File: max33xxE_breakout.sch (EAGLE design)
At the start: 12 parts

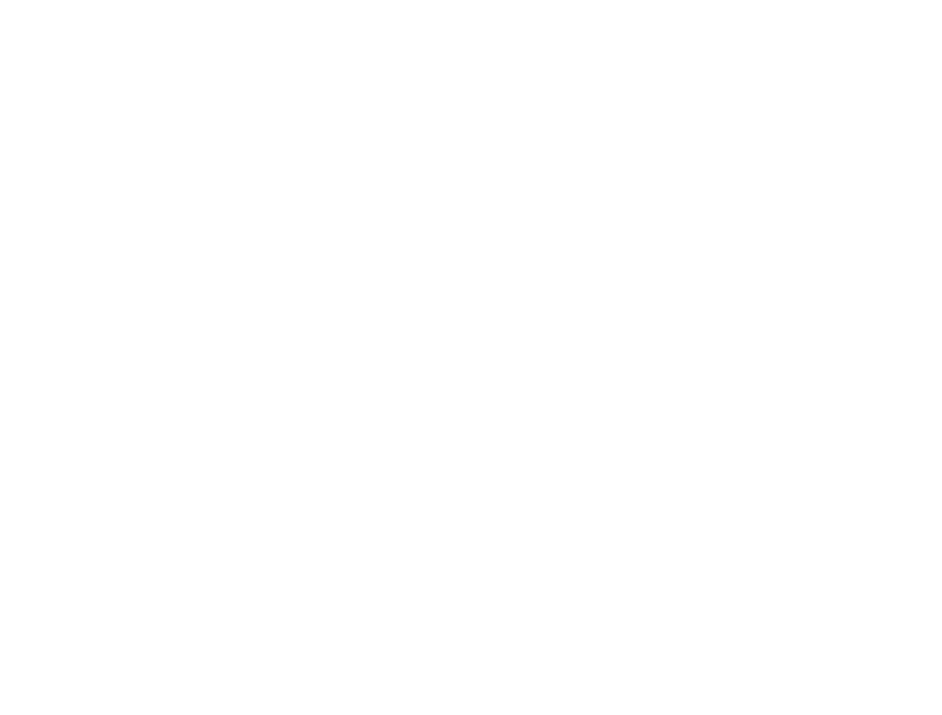
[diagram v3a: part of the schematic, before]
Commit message: remove the cluttering names
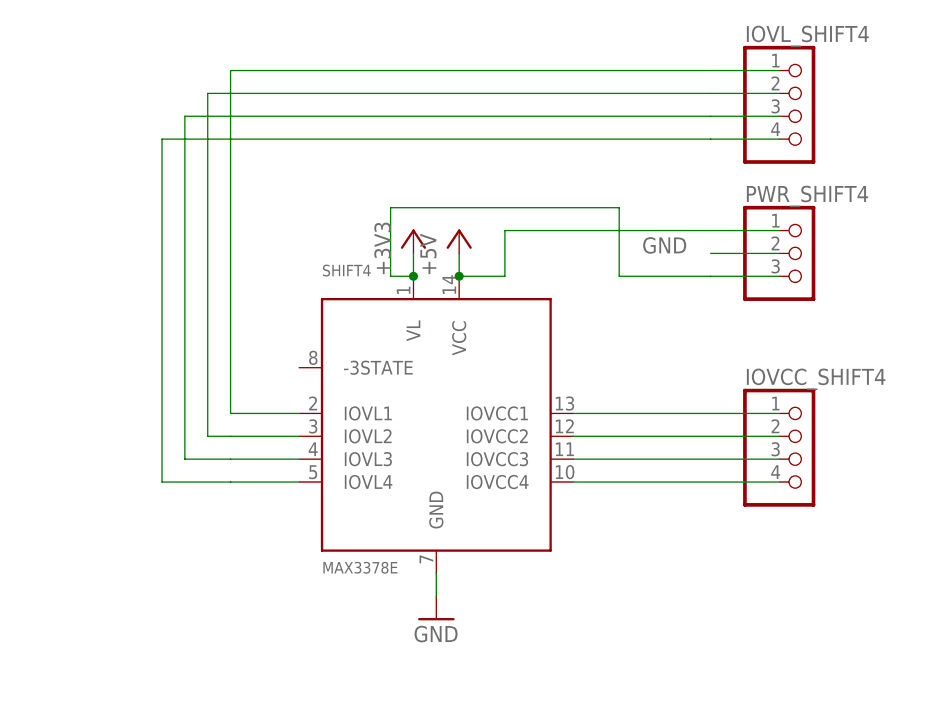
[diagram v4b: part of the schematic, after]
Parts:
- added IOVCC_SHIFT4, IOVL_SHIFT4: (no value), pinhead:PINHD-1X4
- added PWR_SHIFT4: (no value), pinhead:PINHD-1X3
- added SHIFT4: MAX3378E, max33xxE_lvl_shifters:MAX3378E
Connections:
- new net IOVCC1_SHIFT4: IOVCC_SHIFT4.1, SHIFT4.IOVCC1
- new net IOVCC2_SHIFT4: IOVCC_SHIFT4.2, SHIFT4.IOVCC2
- new net IOVCC3_SHIFT4: IOVCC_SHIFT4.3, SHIFT4.IOVCC3
- new net IOVCC4_SHIFT4: IOVCC_SHIFT4.4, SHIFT4.IOVCC4
- new net IOVL1_SHIFT4: IOVL_SHIFT4.1, SHIFT4.IOVL1
- new net IOVL2_SHIFT4: IOVL_SHIFT4.2, SHIFT4.IOVL2
- new net IOVL3_SHIFT4: IOVL_SHIFT4.3, SHIFT4.IOVL3
- new net IOVL4_SHIFT4: IOVL_SHIFT4.4, SHIFT4.IOVL4
- new net VCC_SHIFT4: PWR_SHIFT4.1, SHIFT4.VCC
- new net VL_SHIFT4: PWR_SHIFT4.3, SHIFT4.VL
- net GND: now also PWR_SHIFT4.2, SHIFT4.GND
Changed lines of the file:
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@@
 <part name="IOVCC_SHIFT3" library="pinhead" deviceset="PINHD-1X4" device=""/>
 <part name="IOVL_SHIFT3" library="pinhead" deviceset="PINHD-1X4" device=""/>
+<part name="SHIFT4" library="max33xxE_lvl_shifters" deviceset="MAX3378E" device=""/>
+<part name="GND4" library="supply1" deviceset="GND" device=""/>
+<part name="P+4" library="supply1" deviceset="+5V" device=""/>
+<part name="+3V4" library="supply1" deviceset="+3V3" device=""/>
+<part name="PWR_SHIFT4" library="pinhead" deviceset="PINHD-1X3" device=""/>
+<part name="IOVCC_SHIFT4" library="pinhead" deviceset="PINHD-1X4" device=""/>
+<part name="IOVL_SHIFT4" library="pinhead" deviceset="PINHD-1X4" device=""/>
 </parts>
 <sheets>
@@
 <instance part="IOVCC_SHIFT3" gate="A" x="266.7" y="35.56"/>
 <instance part="IOVL_SHIFT3" gate="A" x="266.7" y="73.66"/>
+<instance part="SHIFT4" gate="G$1" x="325.12" y="43.18"/>
+<instance part="GND4" gate="1" x="325.12" y="22.86"/>
+<instance part="P+4" gate="1" x="327.66" y="66.04"/>
+<instance part="+3V4" gate="G$1" x="322.58" y="66.04"/>
+<instance part="PWR_SHIFT4" gate="A" x="365.76" y="63.5"/>
+<instance part="IOVCC_SHIFT4" gate="A" x="365.76" y="40.64"/>
+<instance part="IOVL_SHIFT4" gate="A" x="365.76" y="78.74"/>
 </instances>
 <busses>
@@
 <wire x1="264.16" y1="58.42" x2="256.54" y2="58.42" width="0.1524" layer="91"/>
 <label x="248.92" y="58.42" size="1.778" layer="95"/>
+</segment>
+<segment>
+<pinref part="SHIFT4" gate="G$1" pin="GND"/>
+<pinref part="GND4" gate="1" pin="GND"/>
+<wire x1="325.12" y1="25.4" x2="325.12" y2="27.94" width="0.1524" layer="91"/>
+</segment>
+<segment>
+<pinref part="PWR_SHIFT4" gate="A" pin="2"/>
+<wire x1="363.22" y1="63.5" x2="355.6" y2="63.5" width="0.1524" layer="91"/>
+<label x="347.98" y="63.5" size="1.778" layer="95"/>
 </segment>
 </net>
@@
 </segment>
 </net>
+<net name="IOVCC4_SHIFT4" class="0">
+<segment>
+<pinref part="SHIFT4" gate="G$1" pin="IOVCC4"/>
+<pinref part="IOVCC_SHIFT4" gate="A" pin="4"/>
+<wire x1="340.36" y1="38.1" x2="363.22" y2="38.1" width="0.1524" layer="91"/>
+</segment>
+</net>
+<net name="IOVCC3_SHIFT4" class="0">
+<segment>
+<pinref part="SHIFT4" gate="G$1" pin="IOVCC3"/>
+<pinref part="IOVCC_SHIFT4" gate="A" pin="3"/>
+<wire x1="340.36" y1="40.64" x2="363.22" y2="40.64" width="0.1524" layer="91"/>
+</segment>
+</net>
+<net name="IOVCC2_SHIFT4" class="0">
+<segment>
+<pinref part="SHIFT4" gate="G$1" pin="IOVCC2"/>
+<pinref part="IOVCC_SHIFT4" gate="A" pin="2"/>
+<wire x1="340.36" y1="43.18" x2="363.22" y2="43.18" width="0.1524" layer="91"/>
+</segment>
+</net>
+<net name="IOVCC1_SHIFT4" class="0">
+<segment>
+<pinref part="SHIFT4" gate="G$1" pin="IOVCC1"/>
+<pinref part="IOVCC_SHIFT4" gate="A" pin="1"/>
+<wire x1="340.36" y1="45.72" x2="363.22" y2="45.72" width="0.1524" layer="91"/>
+</segment>
+</net>
+<net name="IOVL2_SHIFT4" class="0">
+<segment>
+<pinref part="IOVL_SHIFT4" gate="A" pin="2"/>
+<wire x1="363.22" y1="81.28" x2="355.6" y2="81.28" width="0.1524" layer="91"/>
+<wire x1="355.6" y1="81.28" x2="299.72" y2="81.28" width="0.1524" layer="91"/>
+<wire x1="299.72" y1="81.28" x2="299.72" y2="43.18" width="0.1524" layer="91"/>
+<pinref part="SHIFT4" gate="G$1" pin="IOVL2"/>
+<wire x1="309.88" y1="43.18" x2="302.26" y2="43.18" width="0.1524" layer="91"/>
+<wire x1="299.72" y1="43.18" x2="302.26" y2="43.18" width="0.1524" layer="91"/>
+</segment>
+</net>
+<net name="IOVL1_SHIFT4" class="0">
+<segment>
+<pinref part="IOVL_SHIFT4" gate="A" pin="1"/>
+<wire x1="363.22" y1="83.82" x2="355.6" y2="83.82" width="0.1524" layer="91"/>
+<pinref part="SHIFT4" gate="G$1" pin="IOVL1"/>
+<wire x1="309.88" y1="45.72" x2="302.26" y2="45.72" width="0.1524" layer="91"/>
+<wire x1="355.6" y1="83.82" x2="302.26" y2="83.82" width="0.1524" layer="91"/>
+<wire x1="302.26" y1="83.82" x2="302.26" y2="45.72" width="0.1524" layer="91"/>
+</segment>
+</net>
+<net name="IOVL3_SHIFT4" class="0">
+<segment>
+<pinref part="IOVL_SHIFT4" gate="A" pin="3"/>
+<wire x1="363.22" y1="78.74" x2="355.6" y2="78.74" width="0.1524" layer="91"/>
+<wire x1="355.6" y1="78.74" x2="297.18" y2="78.74" width="0.1524" layer="91"/>
+<wire x1="297.18" y1="78.74" x2="297.18" y2="40.64" width="0.1524" layer="91"/>
+<pinref part="SHIFT4" gate="G$1" pin="IOVL3"/>
+<wire x1="309.88" y1="40.64" x2="302.26" y2="40.64" width="0.1524" layer="91"/>
+<wire x1="297.18" y1="40.64" x2="302.26" y2="40.64" width="0.1524" layer="91"/>
+</segment>
+</net>
+<net name="IOVL4_SHIFT4" class="0">
+<segment>
+<pinref part="IOVL_SHIFT4" gate="A" pin="4"/>
+<wire x1="363.22" y1="76.2" x2="355.6" y2="76.2" width="0.1524" layer="91"/>
+<wire x1="355.6" y1="76.2" x2="294.64" y2="76.2" width="0.1524" layer="91"/>
+<wire x1="294.64" y1="76.2" x2="294.64" y2="38.1" width="0.1524" layer="91"/>
+<pinref part="SHIFT4" gate="G$1" pin="IOVL4"/>
+<wire x1="309.88" y1="38.1" x2="302.26" y2="38.1" width="0.1524" layer="91"/>
+<wire x1="294.64" y1="38.1" x2="302.26" y2="38.1" width="0.1524" layer="91"/>
+</segment>
+</net>
+<net name="VL_SHIFT4" class="0">
+<segment>
+<pinref part="SHIFT4" gate="G$1" pin="VL"/>
+<pinref part="+3V4" gate="G$1" pin="+3V3"/>
+<wire x1="322.58" y1="63.5" x2="322.58" y2="60.96" width="0.1524" layer="91"/>
+<pinref part="PWR_SHIFT4" gate="A" pin="3"/>
+<wire x1="363.22" y1="60.96" x2="355.6" y2="60.96" width="0.1524" layer="91"/>
+<wire x1="355.6" y1="60.96" x2="345.44" y2="60.96" width="0.1524" layer="91"/>
+<wire x1="345.44" y1="60.96" x2="345.44" y2="68.58" width="0.1524" layer="91"/>
+<wire x1="345.44" y1="68.58" x2="320.04" y2="68.58" width="0.1524" layer="91"/>
+<wire x1="320.04" y1="68.58" x2="320.04" y2="60.96" width="0.1524" layer="91"/>
+<wire x1="320.04" y1="60.96" x2="322.58" y2="60.96" width="0.1524" layer="91"/>
+<junction x="322.58" y="60.96"/>
+</segment>
+</net>
+<net name="VCC_SHIFT4" class="0">
+<segment>
+<pinref part="SHIFT4" gate="G$1" pin="VCC"/>
+<pinref part="P+4" gate="1" pin="+5V"/>
+<wire x1="327.66" y1="63.5" x2="327.66" y2="60.96" width="0.1524" layer="91"/>
+<pinref part="PWR_SHIFT4" gate="A" pin="1"/>
+<wire x1="363.22" y1="66.04" x2="355.6" y2="66.04" width="0.1524" layer="91"/>
+<wire x1="355.6" y1="66.04" x2="332.74" y2="66.04" width="0.1524" layer="91"/>
+<wire x1="332.74" y1="66.04" x2="332.74" y2="60.96" width="0.1524" layer="91"/>
+<wire x1="332.74" y1="60.96" x2="327.66" y2="60.96" width="0.1524" layer="91"/>
+<junction x="327.66" y="60.96"/>
+</segment>
+</net>

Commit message: bypass caps
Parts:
- added C1, C2, C3, C4, C5, C6, C7, C8: (no value), rcl:C-EUC0603K
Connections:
- net GND: now also C1.2, C2.2, C3.2, C4.2, C5.2, C6.2, C7.2, C8.2
- net VCC_SHIFT1: now also C2.1
- net VCC_SHIFT2: now also C4.1
- net VCC_SHIFT3: now also C6.1
- net VCC_SHIFT4: now also C8.1
- net VL_SHIFT1: now also C1.1
- net VL_SHIFT2: now also C3.1
- net VL_SHIFT3: now also C5.1
- net VL_SHIFT4: now also C7.1
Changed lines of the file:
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@@
 <part name="IOVCC_SHIFT4" library="pinhead" deviceset="PINHD-1X4" device=""/>
 <part name="IOVL_SHIFT4" library="pinhead" deviceset="PINHD-1X4" device=""/>
+<part name="C1" library="rcl" deviceset="C-EU" device="C0603K"/>
+<part name="C2" library="rcl" deviceset="C-EU" device="C0603K"/>
+<part name="C3" library="rcl" deviceset="C-EU" device="C0603K"/>
+<part name="C4" library="rcl" deviceset="C-EU" device="C0603K"/>
+<part name="C5" library="rcl" deviceset="C-EU" device="C0603K"/>
+<part name="C6" library="rcl" deviceset="C-EU" device="C0603K"/>
+<part name="C7" library="rcl" deviceset="C-EU" device="C0603K"/>
+<part name="C8" library="rcl" deviceset="C-EU" device="C0603K"/>
+<part name="GND5" library="supply1" deviceset="GND" device=""/>
+<part name="GND6" library="supply1" deviceset="GND" device=""/>
+<part name="GND7" library="supply1" deviceset="GND" device=""/>
+<part name="GND8" library="supply1" deviceset="GND" device=""/>
+<part name="GND9" library="supply1" deviceset="GND" device=""/>
+<part name="GND10" library="supply1" deviceset="GND" device=""/>
+<part name="GND11" library="supply1" deviceset="GND" device=""/>
+<part name="GND12" library="supply1" deviceset="GND" device=""/>
 </parts>
 <sheets>
@@
 <instance part="IOVCC_SHIFT4" gate="A" x="365.76" y="40.64"/>
 <instance part="IOVL_SHIFT4" gate="A" x="365.76" y="78.74"/>
+<instance part="C1" gate="G$1" x="25.4" y="81.28"/>
+<instance part="C2" gate="G$1" x="38.1" y="81.28"/>
+<instance part="C3" gate="G$1" x="127" y="96.52"/>
+<instance part="C4" gate="G$1" x="137.16" y="96.52"/>
+<instance part="C5" gate="G$1" x="223.52" y="96.52"/>
+<instance part="C6" gate="G$1" x="238.76" y="96.52"/>
+<instance part="C7" gate="G$1" x="320.04" y="99.06"/>
+<instance part="C8" gate="G$1" x="335.28" y="99.06"/>
+<instance part="GND5" gate="1" x="320.04" y="91.44"/>
+<instance part="GND6" gate="1" x="335.28" y="91.44"/>
+<instance part="GND7" gate="1" x="238.76" y="88.9"/>
+<instance part="GND8" gate="1" x="223.52" y="88.9"/>
+<instance part="GND9" gate="1" x="137.16" y="88.9"/>
+<instance part="GND10" gate="1" x="127" y="88.9"/>
+<instance part="GND11" gate="1" x="25.4" y="73.66"/>
+<instance part="GND12" gate="1" x="38.1" y="73.66"/>
 </instances>
 <busses>
@@
 <label x="347.98" y="63.5" size="1.778" layer="95"/>
 </segment>
+<segment>
+<pinref part="C7" gate="G$1" pin="2"/>
+<pinref part="GND5" gate="1" pin="GND"/>
+</segment>
+<segment>
+<pinref part="C8" gate="G$1" pin="2"/>
+<pinref part="GND6" gate="1" pin="GND"/>
+</segment>
+<segment>
+<pinref part="C6" gate="G$1" pin="2"/>
+<pinref part="GND7" gate="1" pin="GND"/>
+</segment>
+<segment>
+<pinref part="C5" gate="G$1" pin="2"/>
+<pinref part="GND8" gate="1" pin="GND"/>
+</segment>
+<segment>
+<pinref part="C4" gate="G$1" pin="2"/>
+<pinref part="GND9" gate="1" pin="GND"/>
+</segment>
+<segment>
+<pinref part="C3" gate="G$1" pin="2"/>
+<pinref part="GND10" gate="1" pin="GND"/>
+</segment>
+<segment>
+<pinref part="C1" gate="G$1" pin="2"/>
+<pinref part="GND11" gate="1" pin="GND"/>
+</segment>
+<segment>
+<pinref part="C2" gate="G$1" pin="2"/>
+<pinref part="GND12" gate="1" pin="GND"/>
+</segment>
 </net>
 <net name="VCC_SHIFT1" class="0">
@@
 <label x="66.04" y="25.4" size="1.778" layer="95" rot="R180"/>
 </segment>
+<segment>
+<pinref part="C2" gate="G$1" pin="1"/>
+<wire x1="38.1" y1="83.82" x2="38.1" y2="88.9" width="0.1524" layer="91"/>
+<label x="35.56" y="86.36" size="1.778" layer="95" rot="R90"/>
+</segment>
 </net>
 <net name="VL_SHIFT1" class="0">
@@
 <wire x1="71.12" y1="17.78" x2="63.5" y2="17.78" width="0.1524" layer="91"/>
 <label x="66.04" y="17.78" size="1.778" layer="95" rot="R180"/>
+</segment>
+<segment>
+<pinref part="C1" gate="G$1" pin="1"/>
+<wire x1="25.4" y1="83.82" x2="25.4" y2="88.9" width="0.1524" layer="91"/>
+<label x="22.86" y="86.36" size="1.778" layer="95" rot="R90"/>
 </segment>
 </net>
@@
 <junction x="127" y="60.96"/>
 </segment>
+<segment>
+<pinref part="C3" gate="G$1" pin="1"/>
+<wire x1="127" y1="99.06" x2="127" y2="104.14" width="0.1524" layer="91"/>
+<label x="124.46" y="101.6" size="1.778" layer="95" rot="R90"/>
+</segment>
 </net>
 <net name="VCC_SHIFT2" class="0">
@@
 <wire x1="137.16" y1="60.96" x2="132.08" y2="60.96" width="0.1524" layer="91"/>
 <junction x="132.08" y="60.96"/>
+</segment>
+<segment>
+<pinref part="C4" gate="G$1" pin="1"/>
+<wire x1="137.16" y1="99.06" x2="137.16" y2="104.14" width="0.1524" layer="91"/>
+<label x="134.62" y="101.6" size="1.778" layer="95" rot="R90"/>
 </segment>
 </net>
@@
 <junction x="223.52" y="55.88"/>
 </segment>
+<segment>
+<pinref part="C5" gate="G$1" pin="1"/>
+<wire x1="223.52" y1="99.06" x2="223.52" y2="104.14" width="0.1524" layer="91"/>
+<label x="220.98" y="104.14" size="1.778" layer="95" rot="R90"/>
+</segment>
 </net>
 <net name="VCC_SHIFT3" class="0">
@@
 <wire x1="233.68" y1="55.88" x2="228.6" y2="55.88" width="0.1524" layer="91"/>
 <junction x="228.6" y="55.88"/>
+</segment>
+<segment>
+<pinref part="C6" gate="G$1" pin="1"/>
+<wire x1="238.76" y1="99.06" x2="238.76" y2="104.14" width="0.1524" layer="91"/>
+<label x="236.22" y="104.14" size="1.778" layer="95" rot="R90"/>
 </segment>
 </net>
@@
 <junction x="322.58" y="60.96"/>
 </segment>
+<segment>
+<pinref part="C7" gate="G$1" pin="1"/>
+<wire x1="320.04" y1="101.6" x2="320.04" y2="109.22" width="0.1524" layer="91"/>
+<label x="317.5" y="106.68" size="1.778" layer="95" rot="R90"/>
+</segment>
 </net>
 <net name="VCC_SHIFT4" class="0">
@@
 <junction x="327.66" y="60.96"/>
 </segment>
-</net>
+<segment>
+<pinref part="C8" gate="G$1" pin="1"/>
+<wire x1="335.28" y1="101.6" x2="335.28" y2="109.22" width="0.1524" layer="91"/>
+<label x="332.74" y="106.68" size="1.778" layer="95" rot="R90"/>
+</segment>
+</net>
